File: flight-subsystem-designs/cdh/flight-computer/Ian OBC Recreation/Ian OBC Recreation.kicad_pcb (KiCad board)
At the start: 4 copper layers, 90.3 x 95.9 mm, 45 parts, among them U1 BEAGLEBONEBLACK, U3 TCAN337G, U4 MCP7940N-xSN, U5 ADM3485EARZ, U6 MAX706RESA+T, U7 TMP36xS

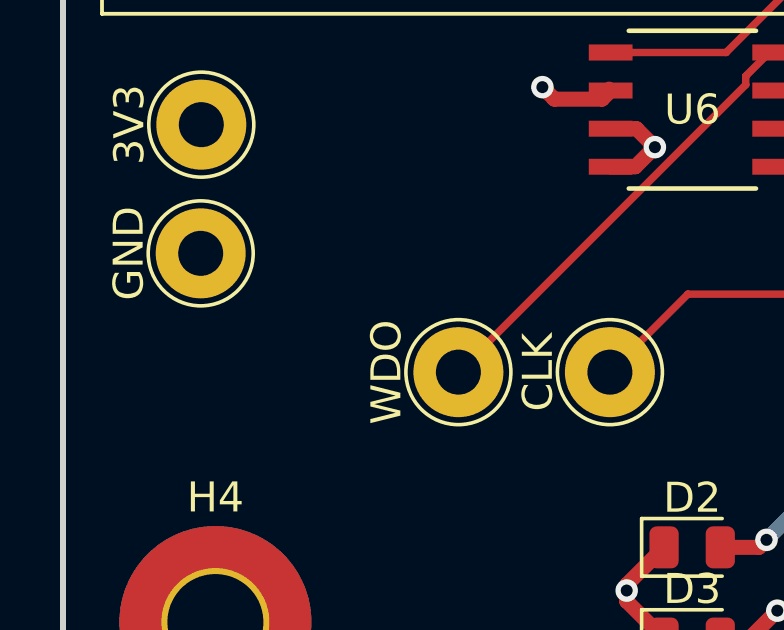
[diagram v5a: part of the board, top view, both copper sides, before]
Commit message: Fixed UART
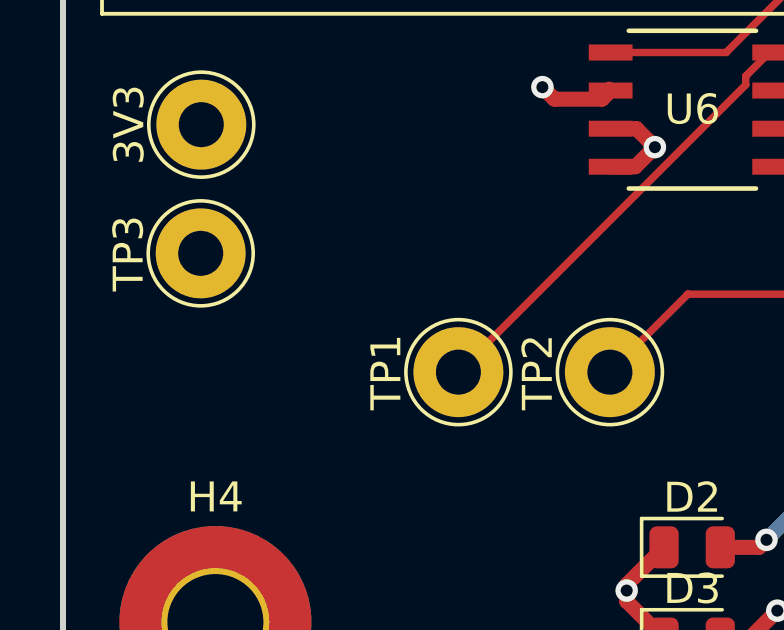
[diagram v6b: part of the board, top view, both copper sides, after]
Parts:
- renumbered WDO to TP1, CLK to TP2, GND to TP3
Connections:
- H5 pad 19: /UART_RX -> /UART_TX
- H5 pad 20: /UART_TX -> /UART_RX
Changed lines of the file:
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@@
 		(descr "THT pad as test Point, diameter 3.0mm, hole diameter 1.5mm")
 		(tags "test point THT pad")
-		(property "Reference" "CLK"
+		(property "Reference" "TP2"
 			(at 0 -2.398 90)
 			(layer "F.SilkS")
@@
 		(descr "THT pad as test Point, diameter 3.0mm, hole diameter 1.5mm")
 		(tags "test point THT pad")
-		(property "Reference" "GND"
+		(property "Reference" "TP3"
 			(at 0 -2.398 90)
 			(layer "F.SilkS")
@@
 		(descr "THT pad as test Point, diameter 3.0mm, hole diameter 1.5mm")
 		(tags "test point THT pad")
-		(property "Reference" "WDO"
+		(property "Reference" "TP1"
 			(at 0 -2.398 90)
 			(layer "F.SilkS")
@@
 			(layers "*.Cu" "*.Mask")
 			(remove_unused_layers no)
-			(net 10 "/UART_RX")
+			(net 9 "/UART_TX")
 			(pinfunction "Pin_19")
 			(pintype "passive")
@@
 			(layers "*.Cu" "*.Mask")
 			(remove_unused_layers no)
-			(net 9 "/UART_TX")
+			(net 10 "/UART_RX")
 			(pinfunction "Pin_20")
 			(pintype "passive")
